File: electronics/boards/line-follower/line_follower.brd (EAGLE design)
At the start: 48 x 48 mm, 33 parts, among them IC1 ATTINY441-SSU, IC3 NCP1117ST50T3G, J1 GROVE_CONNECTOR2.0_1X4, J2 GROVE_CONNECTOR2.0_1X4, J3 10129383-906001ALF, Q1 TCRT5000, Q2 TCRT5000, Q3 TCRT5000, Y1 X322516MLB4SI

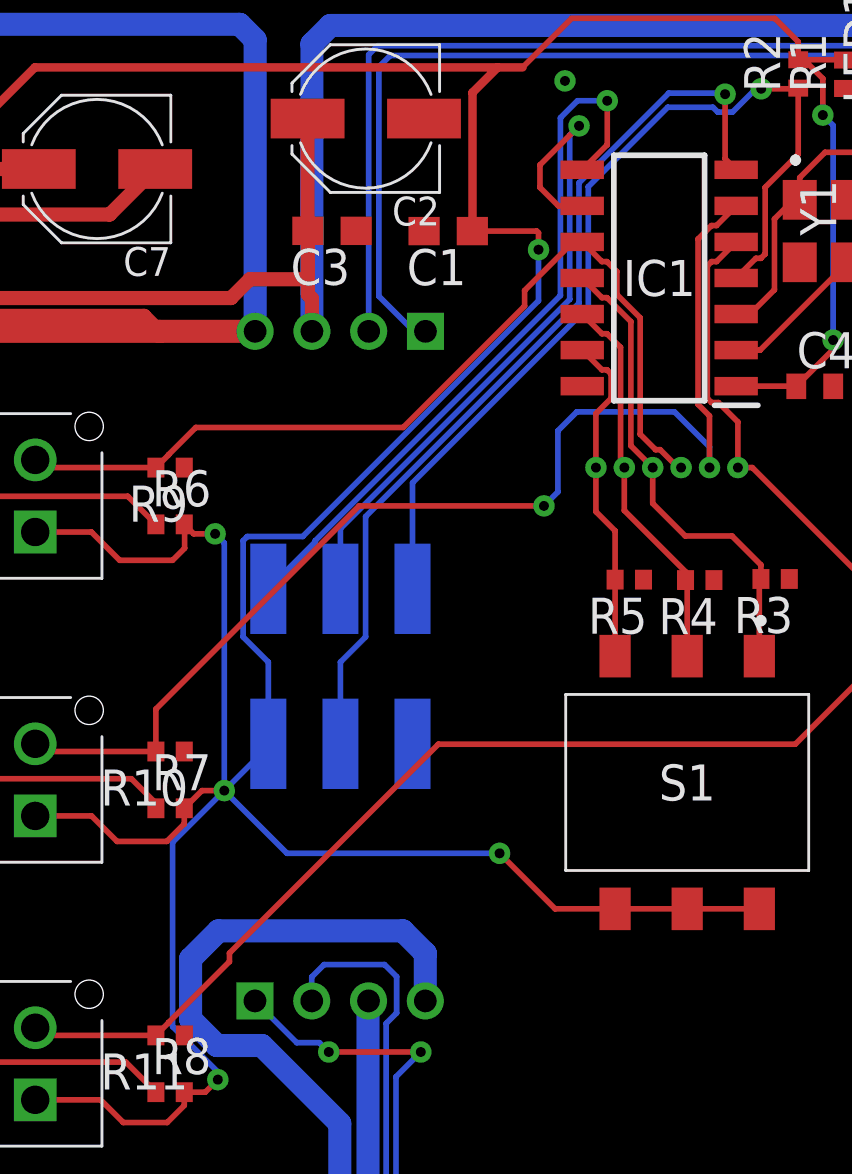
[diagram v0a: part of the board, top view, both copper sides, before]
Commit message: - atmega-Platinen: Stop-Schicht angepasst auf Original - Attiny-Platinen: I2C-Leitungen korrigiert - CAM-Daten für alle Platinen erstellt
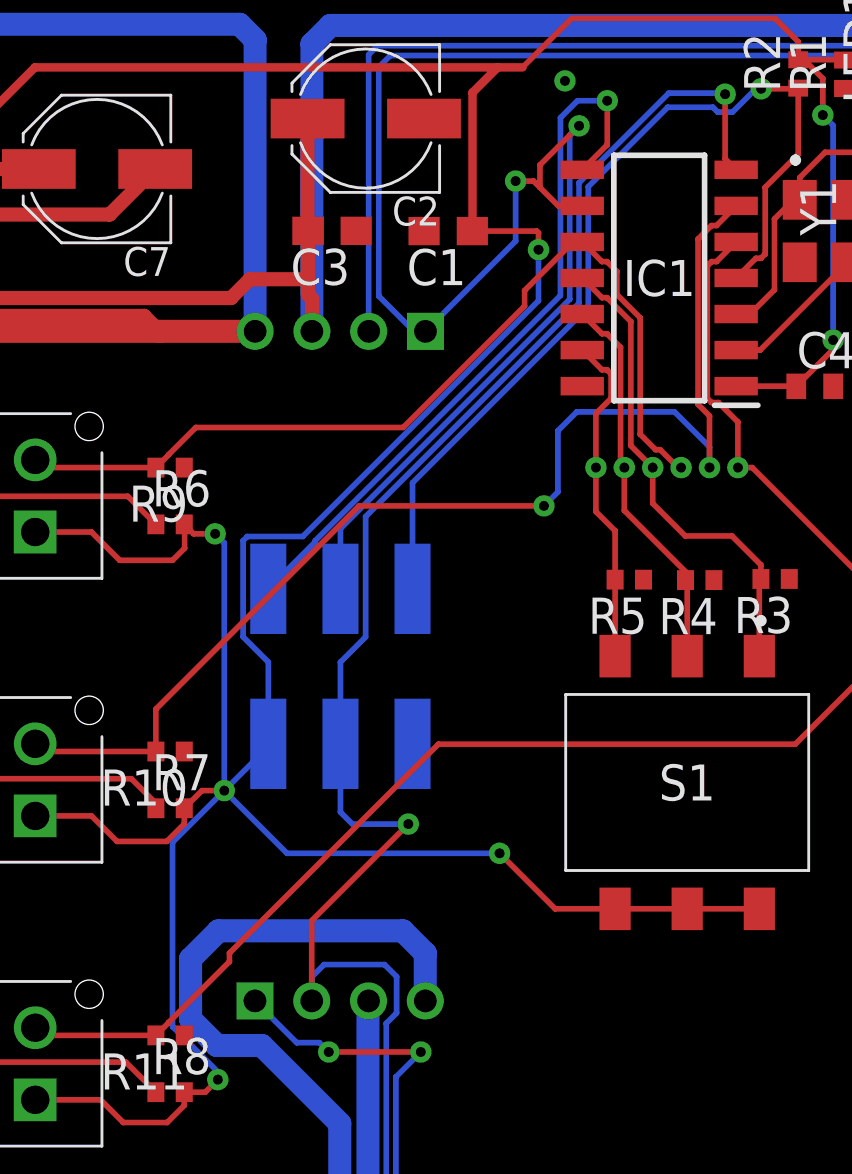
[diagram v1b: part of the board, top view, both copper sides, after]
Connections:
- removed net SCL: J1.1, J2.1
- removed net SDA: J1.2, J2.2
- net MOSI/SDA: now also J1.2, J2.2
- net SCK/SCL: now also J1.1, J2.1
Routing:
- net MOSI/SDA: track 32.6 -> 153.3 mm, vias 1 -> 2
- net SCK/SCL: track 24.3 -> 138.3 mm, vias 1 -> 4
- net SDA: track 108.1 -> 0.00 mm
- net SCL: track 106.5 -> 0.00 mm, vias 2 -> 0
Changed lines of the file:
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@@
 <contactref element="R11" pad="1"/>
-</signal>
-<signal name="SCL">
-<contactref element="J1" pad="1"/>
-<contactref element="J2" pad="1"/>
-<wire x1="20.99033125" y1="12.2144" x2="22.461928125" y2="10.742803125" width="0.2" layer="16"/>
-<wire x1="23.26105625" y1="10.742803125" x2="23.58858125" y2="10.415278125" width="0.2" layer="16"/>
-<via x="23.58858125" y="10.415278125" extent="1-16" drill="0.35"/>
-<via x="26.832009375" y="10.415278125" extent="1-16" drill="0.35"/>
-<wire x1="26.832009375" y1="10.415278125" x2="25.95569375" y2="9.5389625" width="0.2" layer="16"/>
-<wire x1="25.95569375" y1="4.5485625" x2="28.0843625" y2="2.41989375" width="0.2" layer="16"/>
-<wire x1="28.0843625" y1="2.41989375" x2="44.9570875" y2="2.41989375" width="0.2" layer="16"/>
-<wire x1="44.9570875" y1="2.41989375" x2="45.578996875" y2="3.041803125" width="0.2" layer="16"/>
-<wire x1="45.578996875" y1="3.041803125" x2="45.578996875" y2="45.184653125" width="0.2" layer="16"/>
-<wire x1="45.25031875" y1="45.51333125" x2="25.757278125" y2="45.51333125" width="0.2" layer="16"/>
-<wire x1="25.757278125" y1="45.51333125" x2="25.35306875" y2="45.109121875" width="0.2" layer="16"/>
-<wire x1="26.590634375" y1="35.799090625" x2="26.995678125" y2="35.799090625" width="0.2" layer="16"/>
-<wire x1="22.461928125" y1="10.742803125" x2="23.26105625" y2="10.742803125" width="0.2" layer="16"/>
-<wire x1="23.58858125" y1="10.415278125" x2="26.832009375" y2="10.415278125" width="0.2" layer="1"/>
-<wire x1="25.95569375" y1="9.5389625" x2="25.95569375" y2="4.5485625" width="0.2" layer="16"/>
-<wire x1="45.578996875" y1="45.184653125" x2="45.25031875" y2="45.51333125" width="0.2" layer="16"/>
-<wire x1="25.35306875" y1="45.109121875" x2="25.35306875" y2="37.03665625" width="0.2" layer="16"/>
-<wire x1="25.35306875" y1="37.03665625" x2="26.590634375" y2="35.799090625" width="0.2" layer="16"/>
-</signal>
-<signal name="SDA">
-<contactref element="J1" pad="2"/>
-<contactref element="J2" pad="2"/>
-<wire x1="24.995678125" y1="35.799090625" x2="24.995678125" y2="45.54409375" width="0.2" layer="16"/>
-<wire x1="25.310890625" y1="45.85930625" x2="45.526596875" y2="45.85930625" width="0.2" layer="16"/>
-<wire x1="45.526596875" y1="45.85930625" x2="45.909415625" y2="45.4764875" width="0.2" layer="16"/>
-<wire x1="45.909415625" y1="45.4764875" x2="45.909415625" y2="2.881575" width="0.2" layer="16"/>
-<wire x1="45.909415625" y1="2.881575" x2="45.119121875" y2="2.09128125" width="0.2" layer="16"/>
-<wire x1="45.119121875" y1="2.09128125" x2="27.915903125" y2="2.09128125" width="0.2" layer="16"/>
-<wire x1="27.915903125" y1="2.09128125" x2="25.61199375" y2="4.395190625" width="0.2" layer="16"/>
-<wire x1="25.61199375" y1="4.395190625" x2="25.61199375" y2="11.4226875" width="0.2" layer="16"/>
-<wire x1="25.9802" y1="11.79089375" x2="25.9802" y2="13.068228125" width="0.2" layer="16"/>
-<wire x1="25.9802" y1="13.068228125" x2="25.55441875" y2="13.494009375" width="0.2" layer="16"/>
-<wire x1="22.99033125" y1="13.059684375" x2="22.99033125" y2="12.2144" width="0.2" layer="16"/>
-<wire x1="25.61199375" y1="11.4226875" x2="25.9802" y2="11.79089375" width="0.2" layer="16"/>
-<wire x1="25.55441875" y1="13.494009375" x2="23.42465625" y2="13.494009375" width="0.2" layer="16"/>
-<wire x1="23.42465625" y1="13.494009375" x2="22.99033125" y2="13.059684375" width="0.2" layer="16"/>
-<wire x1="24.995678125" y1="45.54409375" x2="25.310890625" y2="45.85930625" width="0.2" layer="16"/>
 </signal>
 <signal name="VCC">
@@
 <wire x1="37.93974375" y1="41.48785625" x2="37.54955625" y2="41.87804375" width="0.2" layer="1"/>
 <wire x1="37.54955625" y1="41.87804375" x2="37.54955625" y2="44.15269375" width="0.2" layer="1"/>
+<contactref element="J1" pad="2"/>
+<contactref element="J2" pad="2"/>
+<wire x1="24.995678125" y1="35.799090625" x2="24.995678125" y2="45.54409375" width="0.2" layer="16"/>
+<wire x1="25.310890625" y1="45.85930625" x2="45.526596875" y2="45.85930625" width="0.2" layer="16"/>
+<wire x1="45.526596875" y1="45.85930625" x2="45.909415625" y2="45.4764875" width="0.2" layer="16"/>
+<wire x1="45.909415625" y1="45.4764875" x2="45.909415625" y2="2.881575" width="0.2" layer="16"/>
+<wire x1="45.909415625" y1="2.881575" x2="45.119121875" y2="2.09128125" width="0.2" layer="16"/>
+<wire x1="45.119121875" y1="2.09128125" x2="27.915903125" y2="2.09128125" width="0.2" layer="16"/>
+<wire x1="27.915903125" y1="2.09128125" x2="25.61199375" y2="4.395190625" width="0.2" layer="16"/>
+<wire x1="25.61199375" y1="4.395190625" x2="25.61199375" y2="11.4226875" width="0.2" layer="16"/>
+<wire x1="25.9802" y1="11.79089375" x2="25.9802" y2="13.068228125" width="0.2" layer="16"/>
+<wire x1="25.9802" y1="13.068228125" x2="25.55441875" y2="13.494009375" width="0.2" layer="16"/>
+<wire x1="22.99033125" y1="13.059684375" x2="22.99033125" y2="12.2144" width="0.2" layer="16"/>
+<wire x1="25.61199375" y1="11.4226875" x2="25.9802" y2="11.79089375" width="0.2" layer="16"/>
+<wire x1="25.55441875" y1="13.494009375" x2="23.42465625" y2="13.494009375" width="0.2" layer="16"/>
+<wire x1="23.42465625" y1="13.494009375" x2="22.99033125" y2="13.059684375" width="0.2" layer="16"/>
+<wire x1="24.995678125" y1="45.54409375" x2="25.310890625" y2="45.85930625" width="0.2" layer="16"/>
+<wire x1="22.99033125" y1="12.2144" x2="22.99033125" y2="15.04305625" width="0.2" layer="1"/>
+<wire x1="22.99033125" y1="15.04305625" x2="26.39105" y2="18.443775" width="0.2" layer="1"/>
+<via x="26.39105" y="18.443775" extent="1-16" drill="0.35"/>
+<wire x1="26.39105" y1="18.443775" x2="24.423825" y2="18.443775" width="0.2" layer="16"/>
+<wire x1="24" y1="18.8676" x2="24" y2="21.27" width="0.2" layer="16"/>
+<wire x1="24.423825" y1="18.443775" x2="24" y2="18.8676" width="0.2" layer="16"/>
 </signal>
 <signal name="SCK/SCL">
@@
 <wire x1="31.028328125" y1="40.86558125" x2="31.028328125" y2="41.658715625" width="0.2" layer="1"/>
 <wire x1="31.028328125" y1="41.658715625" x2="32.405578125" y2="43.035965625" width="0.2" layer="1"/>
+<contactref element="J1" pad="1"/>
+<contactref element="J2" pad="1"/>
+<wire x1="20.99033125" y1="12.2144" x2="22.461928125" y2="10.742803125" width="0.2" layer="16"/>
+<wire x1="23.26105625" y1="10.742803125" x2="23.58858125" y2="10.415278125" width="0.2" layer="16"/>
+<via x="23.58858125" y="10.415278125" extent="1-16" drill="0.35"/>
+<via x="26.832009375" y="10.415278125" extent="1-16" drill="0.35"/>
+<wire x1="26.832009375" y1="10.415278125" x2="25.95569375" y2="9.5389625" width="0.2" layer="16"/>
+<wire x1="25.95569375" y1="4.5485625" x2="28.0843625" y2="2.41989375" width="0.2" layer="16"/>
+<wire x1="28.0843625" y1="2.41989375" x2="44.9570875" y2="2.41989375" width="0.2" layer="16"/>
+<wire x1="44.9570875" y1="2.41989375" x2="45.578996875" y2="3.041803125" width="0.2" layer="16"/>
+<wire x1="45.578996875" y1="3.041803125" x2="45.578996875" y2="45.184653125" width="0.2" layer="16"/>
+<wire x1="45.25031875" y1="45.51333125" x2="25.757278125" y2="45.51333125" width="0.2" layer="16"/>
+<wire x1="25.757278125" y1="45.51333125" x2="25.35306875" y2="45.109121875" width="0.2" layer="16"/>
+<wire x1="26.590634375" y1="35.799090625" x2="26.995678125" y2="35.799090625" width="0.2" layer="16"/>
+<wire x1="22.461928125" y1="10.742803125" x2="23.26105625" y2="10.742803125" width="0.2" layer="16"/>
+<wire x1="23.58858125" y1="10.415278125" x2="26.832009375" y2="10.415278125" width="0.2" layer="1"/>
+<wire x1="25.95569375" y1="9.5389625" x2="25.95569375" y2="4.5485625" width="0.2" layer="16"/>
+<wire x1="45.578996875" y1="45.184653125" x2="45.25031875" y2="45.51333125" width="0.2" layer="16"/>
+<wire x1="25.35306875" y1="45.109121875" x2="25.35306875" y2="37.03665625" width="0.2" layer="16"/>
+<wire x1="25.35306875" y1="37.03665625" x2="26.590634375" y2="35.799090625" width="0.2" layer="16"/>
+<wire x1="26.995678125" y1="35.799090625" x2="30.170846875" y2="38.974259375" width="0.2" layer="16"/>
+<wire x1="30.170846875" y1="38.974259375" x2="30.170846875" y2="41.091375" width="0.2" layer="16"/>
+<via x="30.170846875" y="41.091375" extent="1-16" drill="0.35"/>
+<wire x1="30.170846875" y1="41.091375" x2="30.802534375" y2="41.091375" width="0.2" layer="1"/>
+<wire x1="30.802534375" y1="41.091375" x2="31.028328125" y2="40.86558125" width="0.2" layer="1"/>
 </signal>
 <signal name="RESET">
